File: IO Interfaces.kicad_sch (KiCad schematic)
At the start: 63 parts, among them J2 MIDI OUT, J3 MIDI IN, J4 DB25_Socket, J5 DB25_Pins, J6 Keyboard, U10 MC68901, U13 74LS04, U14 74HC164, U15 74LS86, U16 TL497A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

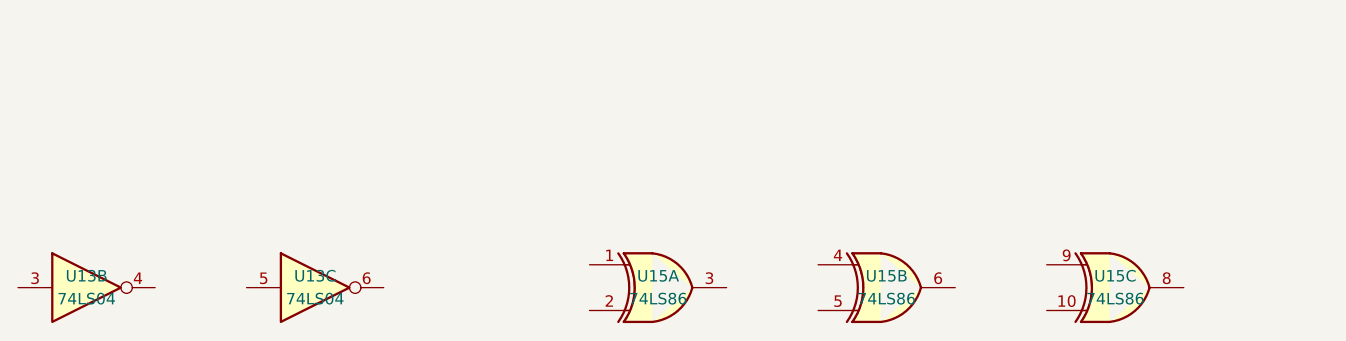
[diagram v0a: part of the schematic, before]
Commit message: motherboard: Added SHIFTER to the schematic and tidied up a pile
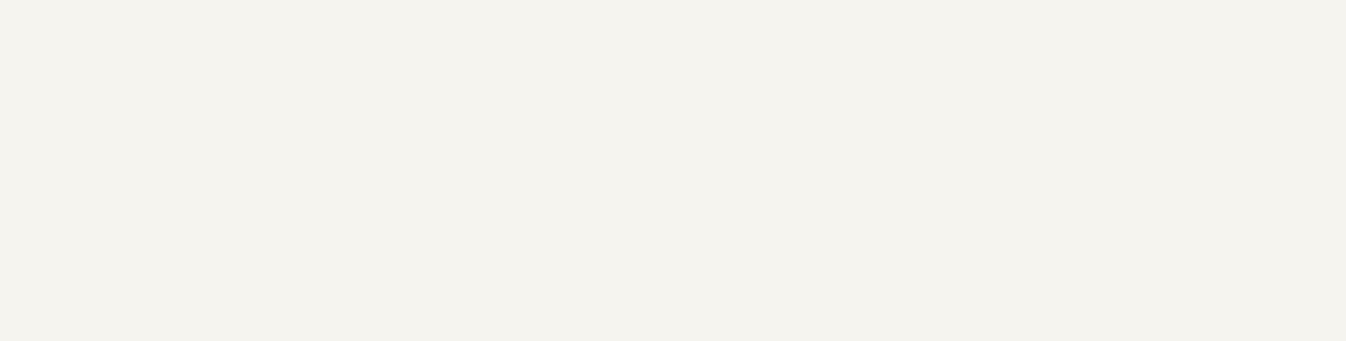
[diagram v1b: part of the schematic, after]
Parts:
- removed unit 2 of U13
- removed unit 3 of U13
- removed unit 2 of U15
- removed unit 1 of U15
- removed unit 3 of U15

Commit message: motherboard: More signal routing, and starting in on the BoM
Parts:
- U6: value 74LS06 -> 74LS05; footprint (none) -> Package_SO:SO-14_3.9x8.65mm_P1.27mm; MFR (none) -> TI; MPN (none) -> SN74HC05DR; OC_FARNELL (none) -> 3120437

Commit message: motherboard: Begun routing the internal floppy disk interface
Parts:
- U6: footprint Package_SO:SO-14_3.9x8.65mm_P1.27mm -> rhais_package-smd:SO-14_3.9x8.65mm_P1.27mm
- U9: footprint Package_DIP:DIP-40_W15.24mm -> rhais_package-dip:DIP-40_W15.24mm_Socket
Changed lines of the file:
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@@
 			)
 		)
-		(property "Footprint" "Package_SO:SO-14_3.9x8.65mm_P1.27mm"
+		(property "Footprint" "rhais_package-smd:SO-14_3.9x8.65mm_P1.27mm"
 			(at 317.5 38.1 0)
 			(effects
@@
 			)
 		)
-		(property "Footprint" "Package_SO:SO-14_3.9x8.65mm_P1.27mm"
+		(property "Footprint" "rhais_package-smd:SO-14_3.9x8.65mm_P1.27mm"
 			(at 342.9 48.26 0)
 			(effects
@@
 			)
 		)
-		(property "Footprint" "Package_DIP:DIP-40_W15.24mm"
+		(property "Footprint" "rhais_package-dip:DIP-40_W15.24mm_Socket"
 			(at 308.61 231.14 0)
 			(effects
@@
 			)
 		)
-		(property "Footprint" "Package_SO:SO-14_3.9x8.65mm_P1.27mm"
+		(property "Footprint" "rhais_package-smd:SO-14_3.9x8.65mm_P1.27mm"
 			(at 342.9 38.1 0)
 			(effects
@@
 			)
 		)
-		(property "Footprint" "Package_SO:SO-14_3.9x8.65mm_P1.27mm"
+		(property "Footprint" "rhais_package-smd:SO-14_3.9x8.65mm_P1.27mm"
 			(at 317.5 48.26 0)
 			(effects
@@
 			)
 		)
-		(property "Footprint" "Package_SO:SO-14_3.9x8.65mm_P1.27mm"
+		(property "Footprint" "rhais_package-smd:SO-14_3.9x8.65mm_P1.27mm"
 			(at 279.4 254 0)
 			(effects

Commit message: motherboard: Begun routing the FM synth sound chip
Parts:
- U13: footprint (none) -> rhais_package-smd:SO-14_3.9x8.65mm_P1.27mm; MFR (none) -> Nexperia; MPN (none) -> 74HCT14D,653; OC_FARNELL (none) -> 1201304
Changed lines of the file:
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@@
 			)
 		)
-		(property "Footprint" ""
+		(property "Footprint" "rhais_package-smd:SO-14_3.9x8.65mm_P1.27mm"
 			(at 101.6 254 0)
 			(effects
@@
 			)
 		)
-		(property "Datasheet" "http://www.ti.com/lit/gpn/sn74LS04"
+		(property "Datasheet" "https://assets.nexperia.com/documents/data-sheet/74HC_HCT14.pdf"
 			(at 101.6 254 0)
 			(effects
@@
 			)
 		)
+		(property "MFR" "Nexperia"
+			(at 101.6 254 0)
+			(effects
+				(font
+					(size 1.27 1.27)
+				)
+				(hide yes)
+			)
+		)
+		(property "MPN" "74HCT14D,653"
+			(at 101.6 254 0)
+			(effects
+				(font
+					(size 1.27 1.27)
+				)
+				(hide yes)
+			)
+		)
+		(property "OC_FARNELL" "1201304"
+			(at 101.6 254 0)
+			(effects
+				(font
+					(size 1.27 1.27)
+				)
+				(hide yes)
+			)
+		)
 		(pin "12"
 		)
@@
 			)
 		)
-		(property "Footprint" ""
+		(property "Footprint" "rhais_package-smd:SO-14_3.9x8.65mm_P1.27mm"
 			(at 254 254 0)
 			(effects
@@
 			)
 		)
-		(property "Datasheet" "http://www.ti.com/lit/gpn/sn74LS04"
+		(property "Datasheet" "https://assets.nexperia.com/documents/data-sheet/74HC_HCT14.pdf"
 			(at 254 254 0)
 			(effects
@@
 			)
 		)
+		(property "MFR" "Nexperia"
+			(at 254 254 0)
+			(effects
+				(font
+					(size 1.27 1.27)
+				)
+				(hide yes)
+			)
+		)
+		(property "MPN" "74HCT14D,653"
+			(at 254 254 0)
+			(effects
+				(font
+					(size 1.27 1.27)
+				)
+				(hide yes)
+			)
+		)
+		(property "OC_FARNELL" "1201304"
+			(at 254 254 0)
+			(effects
+				(font
+					(size 1.27 1.27)
+				)
+				(hide yes)
+			)
+		)
 		(pin "12"
 		)
@@
 			)
 		)
-		(property "Footprint" ""
+		(property "Footprint" "rhais_package-smd:SO-14_3.9x8.65mm_P1.27mm"
 			(at 254 241.3 0)
 			(effects
@@
 			)
 		)
-		(property "Datasheet" "http://www.ti.com/lit/gpn/sn74LS04"
+		(property "Datasheet" "https://assets.nexperia.com/documents/data-sheet/74HC_HCT14.pdf"
 			(at 254 241.3 0)
 			(effects
@@
 			)
 		)
+		(property "MFR" "Nexperia"
+			(at 254 241.3 0)
+			(effects
+				(font
+					(size 1.27 1.27)
+				)
+				(hide yes)
+			)
+		)
+		(property "MPN" "74HCT14D,653"
+			(at 254 241.3 0)
+			(effects
+				(font
+					(size 1.27 1.27)
+				)
+				(hide yes)
+			)
+		)
+		(property "OC_FARNELL" "1201304"
+			(at 254 241.3 0)
+			(effects
+				(font
+					(size 1.27 1.27)
+				)
+				(hide yes)
+			)
+		)
 		(pin "12"
 		)
@@
 			)
 		)
-		(property "Footprint" ""
+		(property "Footprint" "rhais_package-smd:SO-14_3.9x8.65mm_P1.27mm"
 			(at 228.6 254 0)
 			(effects
@@
 			)
 		)
-		(property "Datasheet" "http://www.ti.com/lit/gpn/sn74LS04"
+		(property "Datasheet" "https://assets.nexperia.com/documents/data-sheet/74HC_HCT14.pdf"
 			(at 228.6 254 0)
 			(effects
@@
 			)
 		)
+		(property "MFR" "Nexperia"
+			(at 228.6 254 0)
+			(effects
+				(font
+					(size 1.27 1.27)
+				)
+				(hide yes)
+			)
+		)
+		(property "MPN" "74HCT14D,653"
+			(at 228.6 254 0)
+			(effects
+				(font
+					(size 1.27 1.27)
+				)
+				(hide yes)
+			)
+		)
+		(property "OC_FARNELL" "1201304"
+			(at 228.6 254 0)
+			(effects
+				(font
+					(size 1.27 1.27)
+				)
+				(hide yes)
+			)
+		)
 		(pin "12"
 		)
@@
 			)
 		)
-		(property "Footprint" ""
+		(property "Footprint" "rhais_package-smd:SO-14_3.9x8.65mm_P1.27mm"
 			(at 254 266.7 0)
 			(effects
@@
 			)
 		)
-		(property "Datasheet" "http://www.ti.com/lit/gpn/sn74LS04"
+		(property "Datasheet" "https://assets.nexperia.com/documents/data-sheet/74HC_HCT14.pdf"
 			(at 254 266.7 0)
 			(effects
@@
 			(at 254 266.7 0)
 			(effects
+				(font
+					(size 1.27 1.27)
+				)
+				(hide yes)
+			)
+		)
+		(property "MFR" "Nexperia"
+			(at 254 266.7 0)
+			(effects
+				(font
+					(size 1.27 1.27)
+				)
+				(hide yes)
+			)
+		)
+		(property "MPN" "74HCT14D,653"
+			(at 254 266.7 0)
+			(effects
+				(font
+					(size 1.27 1.27)
+				)
+				(hide yes)
+			)
+		)
+		(property "OC_FARNELL" "1201304"
+			(at 254 266.7 0)
+			(effects

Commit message: motherboard: Routed one of the parallel interfaces and the ROMs
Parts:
- U10: footprint (none) -> Package_DIP:DIP-48_W15.24mm_Socket
- U7, U8: footprint Package_DIP:DIP-24_W15.24mm -> rhais_package-dip:DIP-24_W15.24mm_Socket
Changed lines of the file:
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@@
 			)
 		)
-		(property "Footprint" ""
+		(property "Footprint" "Package_DIP:DIP-48_W15.24mm_Socket"
 			(at 177.8 165.1 0)
 			(effects
@@
 			)
 		)
-		(property "Footprint" "Package_DIP:DIP-24_W15.24mm"
+		(property "Footprint" "rhais_package-dip:DIP-24_W15.24mm_Socket"
 			(at 255.27 92.71 0)
 			(effects
@@
 			)
 		)
-		(property "Footprint" "Package_DIP:DIP-24_W15.24mm"
+		(property "Footprint" "rhais_package-dip:DIP-24_W15.24mm_Socket"
 			(at 179.07 92.71 0)
 			(effects

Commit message: motherboard: Fixed the floppy power connector and defined the board parameters for manufacture
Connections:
- net GND: now also U9.39 (TEST1)
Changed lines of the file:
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@@
 	)
 	(junction
+		(at 276.86 218.44)
+		(diameter 0)
+		(color 0 0 0 0)
+	)
+	(junction
 		(at 38.1 124.46)
 		(diameter 0)
@@
 	(wire
 		(pts
+			(xy 276.86 218.44) (xy 279.4 218.44)
+		)
+		(stroke
+			(width 0)
+			(type default)
+		)
+	)
+	(wire
+		(pts
 			(xy 203.2 142.24) (xy 203.2 144.78)
 		)
@@
 	(wire
 		(pts
+			(xy 276.86 218.44) (xy 276.86 220.98)
+		)
+		(stroke
+			(width 0)
+			(type default)
+		)
+	)
+	(wire
+		(pts
 			(xy 114.3 231.14) (xy 114.3 254)
 		)
@@
 	(wire
 		(pts
-			(xy 276.86 195.58) (xy 276.86 220.98)
+			(xy 276.86 195.58) (xy 276.86 218.44)
 		)
 		(stroke

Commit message: motherboard: Added packaging and ordering information for many of the 7400 logic parts and the DACs
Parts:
- U13: value 74LS04 -> 74HCT14D
- U15: value 74LS86 -> 74HC86; footprint (none) -> rhais_package-smd:SO-14_3.9x8.65mm_P1.27mm; MFR (none) -> Nexperia; MPN (none) -> 74HC86D,653; OC_FARNELL (none) -> 1085331
- U6: value 74LS05 -> 74HS05
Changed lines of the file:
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@@
 			)
 		)
-		(property "Value" "74LS04"
+		(property "Value" "74HCT14D"
 			(at 101.854 248.92 0)
 			(effects
@@
 			)
 		)
-		(property "Value" "74LS05"
+		(property "Value" "74HS05"
 			(at 317.5 33.02 0)
 			(effects
@@
 			)
 		)
-		(property "Value" "74LS04"
+		(property "Value" "74HCT14D"
 			(at 254 248.92 0)
 			(effects
@@
 			)
 		)
-		(property "Value" "74LS86"
+		(property "Value" "74HC86"
 			(at 210.82 255.27 0)
 			(effects
@@
 			)
 		)
-		(property "Footprint" ""
+		(property "Footprint" "rhais_package-smd:SO-14_3.9x8.65mm_P1.27mm"
 			(at 210.82 254 0)
 			(effects
@@
 			)
 		)
-		(property "Datasheet" "74xx/74ls86.pdf"
+		(property "Datasheet" "https://assets.nexperia.com/documents/data-sheet/74HC_HCT86.pdf"
 			(at 210.82 254 0)
 			(effects
@@
 			)
 		)
+		(property "MFR" "Nexperia"
+			(at 210.82 254 0)
+			(effects
+				(font
+					(size 1.27 1.27)
+				)
+				(hide yes)
+			)
+		)
+		(property "MPN" "74HC86D,653"
+			(at 210.82 254 0)
+			(effects
+				(font
+					(size 1.27 1.27)
+				)
+				(hide yes)
+			)
+		)
+		(property "OC_FARNELL" "1085331"
+			(at 210.82 254 0)
+			(effects
+				(font
+					(size 1.27 1.27)
+				)
+				(hide yes)
+			)
+		)
 		(pin "12"
 		)
@@
 			)
 		)
-		(property "Value" "74LS04"
+		(property "Value" "74HCT14D"
 			(at 254 236.22 0)
 			(effects
@@
 			)
 		)
-		(property "Value" "74LS05"
+		(property "Value" "74HS05"
 			(at 342.9 53.34 0)
 			(effects
@@
 			)
 		)
-		(property "Value" "74LS04"
+		(property "Value" "74HCT14D"
 			(at 228.6 255.27 0)
 			(effects
@@
 			)
 		)
-		(property "Value" "74LS05"
+		(property "Value" "74HS05"
 			(at 342.9 33.02 0)
 			(effects
@@
 			)
 		)
-		(property "Value" "74LS05"
+		(property "Value" "74HS05"
 			(at 317.5 53.34 0)
 			(effects
@@
 			)
 		)
-		(property "Value" "74LS05"
+		(property "Value" "74HS05"
 			(at 279.4 255.27 0)
 			(effects
@@
 			)
 		)
-		(property "Value" "74LS86"
+		(property "Value" "74HC86"
 			(at 152.4 251.46 0)
 			(effects
@@
 			)
 		)
-		(property "Footprint" ""
+		(property "Footprint" "rhais_package-smd:SO-14_3.9x8.65mm_P1.27mm"
 			(at 152.4 256.54 0)
 			(effects
@@
 			)
 		)
-		(property "Datasheet" "74xx/74ls86.pdf"
+		(property "Datasheet" "https://assets.nexperia.com/documents/data-sheet/74HC_HCT86.pdf"
 			(at 152.4 256.54 0)
 			(effects
@@
 			)
 		)
+		(property "MFR" "Nexperia"
+			(at 152.4 256.54 0)
+			(effects
+				(font
+					(size 1.27 1.27)
+				)
+				(hide yes)
+			)
+		)
+		(property "MPN" "74HC86D,653"
+			(at 152.4 256.54 0)
+			(effects
+				(font
+					(size 1.27 1.27)
+				)
+				(hide yes)
+			)
+		)
+		(property "OC_FARNELL" "1085331"
+			(at 152.4 256.54 0)
+			(effects
+				(font
+					(size 1.27 1.27)
+				)
+				(hide yes)
+			)
+		)
 		(pin "12"
 		)
@@
 			)
 		)
-		(property "Value" "74LS04"
+		(property "Value" "74HCT14D"
 			(at 254 261.62 0)
 			(effects
